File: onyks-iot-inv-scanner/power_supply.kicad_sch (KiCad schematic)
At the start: 47 parts, among them IC1 TPS22953DSQR, IC2 TPS22953DSQR, IC3 SN74LVC1G06DBVT, IC5 TPS63021DSJR, Q1 DMN3150L, Q2 DMN3150L, U1 DW01A, U3 TP4056-42-ESOP8, U4 TPS62A02ADRL, U5 TPS62A02ADRL

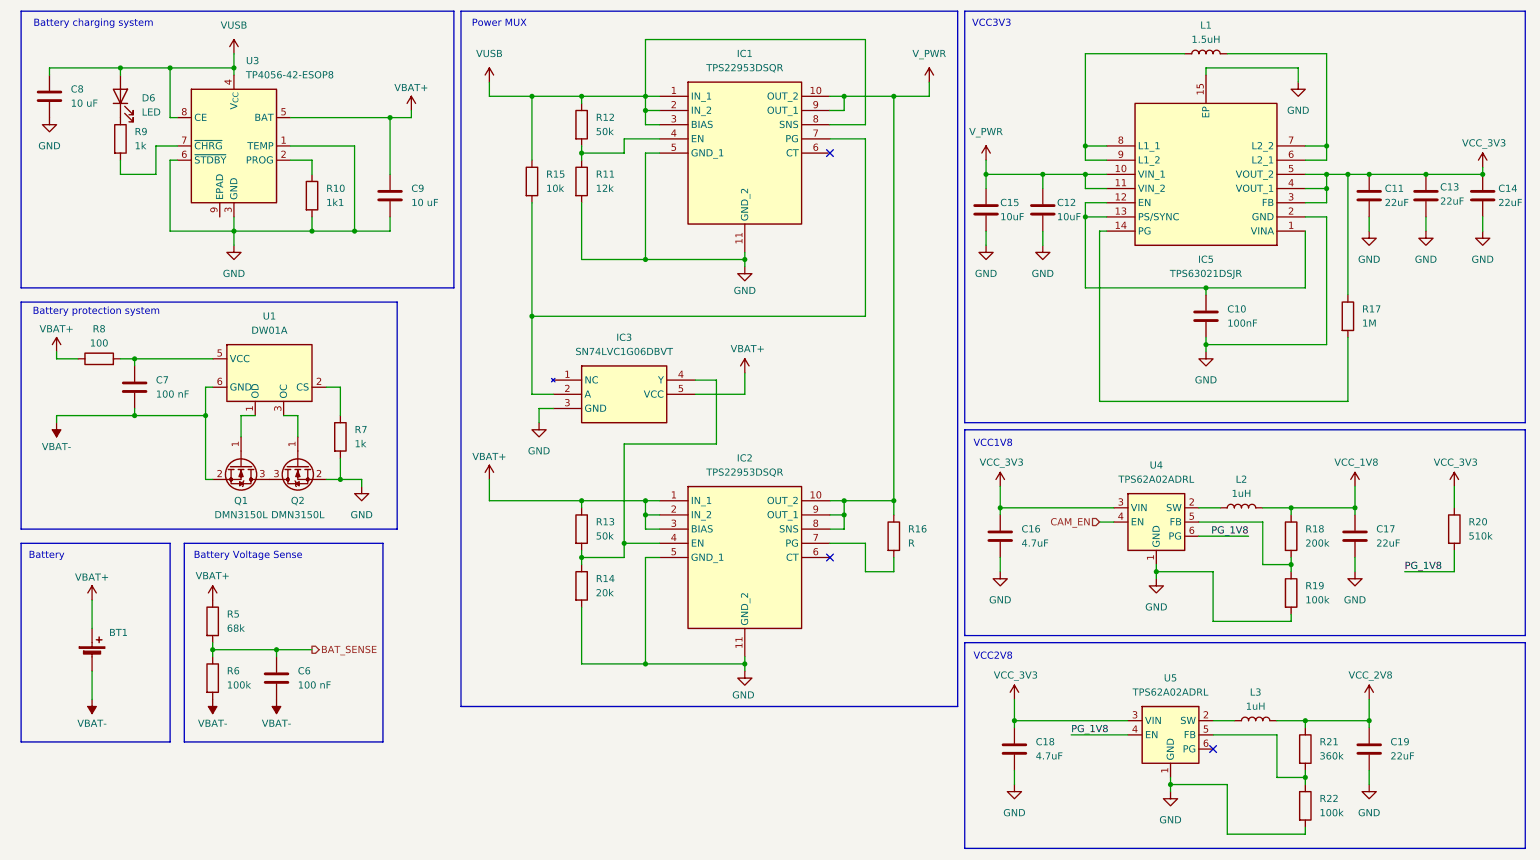
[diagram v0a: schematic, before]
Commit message: unpin usb data lines from battery management IC, becouse of possibly jamming signal
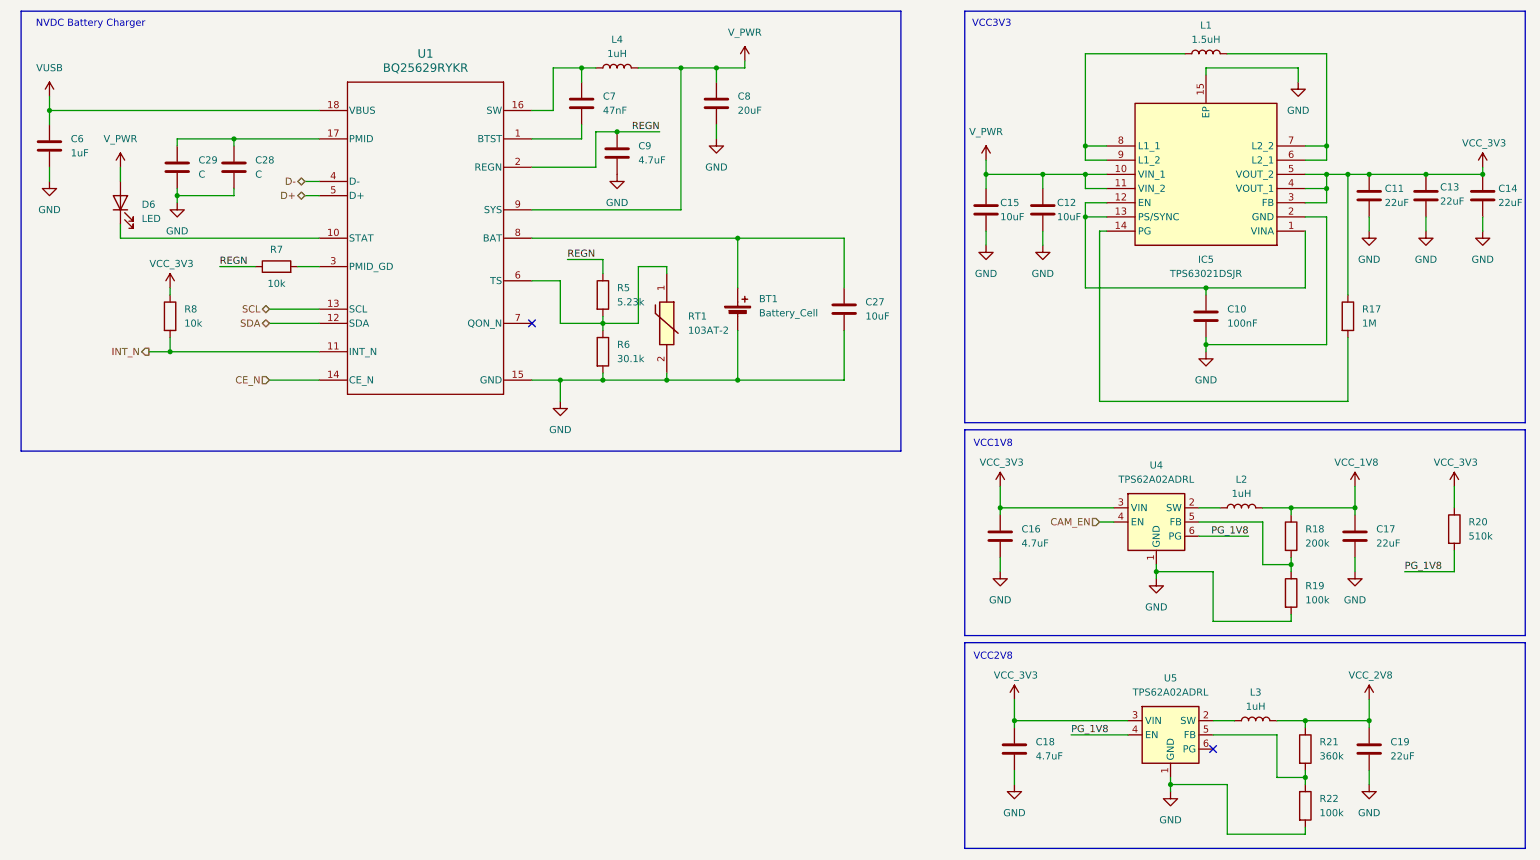
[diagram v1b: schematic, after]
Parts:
- removed IC1, IC2: TPS22953DSQR, Samacsys:SON40P200X200X80-11N, symbol Samacsys:TPS22953DSQR
- removed IC3: SN74LVC1G06DBVT, Samacsys:SOT95P280X145-5N, symbol Samacsys:SN74LVC1G06DBVT
- removed Q1, Q2: DMN3150L, Package_TO_SOT_SMD:SOT-23, symbol Transistor_FET:DMN3150L
- removed R10: 1k1, symbol Device:R
- removed R11: 12k, symbol Device:R
- removed R12, R13: 50k, symbol Device:R
- removed R14: 20k, symbol Device:R
- removed R15: 10k, symbol Device:R
- removed R16: R, symbol Device:R
- removed R9: 1k, symbol Device:R
- removed U1: DW01A, Package_TO_SOT_SMD:SOT-23-6, symbol Battery_Management:DW01A
- removed U3: TP4056-42-ESOP8, Package_SO:SOIC-8-1EP_3.9x4.9mm_P1.27mm_EP2.41x3.3mm_ThermalVias, symbol Battery_Management:TP4056-42-ESOP8
- added C27: 10uF, symbol Device:C
- added C28, C29: C, symbol Device:C
- added L4: 1uH, symbol Device:L
- added RT1: 103AT-2, Samacsys:103AT2, symbol Samacsys:103AT-2
- added U1: BQ25629RYKR, Snapeda:RYK0018A-MFG, symbol Snapeda:BQ25629RYKR
- C6: value 100 nF -> 1uF
- C7: value 100 nF -> 47nF
- C8: value 10 uF -> 20uF
- C9: value 10 uF -> 4.7uF
- R5: value 68k -> 5.23k
- R6: value 100k -> 30.1k
- R7: value 1k -> 10k
- R8: value 100 -> 10k
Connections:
- net GND: now also BT1.2 (-), C6.2, R6.2, C27.2, C28.2, C29.2, RT1.2, U1.15 (GND); no longer R7.2
- net VCC_3V3: now also R8.1
- net VUSB: now also C6.1, U1.18 (VBUS); no longer C8.1, D6.2 (A)
- net V_PWR: now also C8.1, D6.2 (A), L4.2, U1.9 (SYS)
- net REGN: now reaches R7.1
- net REGN: now also C9.1, R5.1, U1.2 (REGN)
- net at C7.1: now also L4.1, U1.16 (SW); no longer R8.2
- net at D6.1 (K): now also U1.10 (STAT)
- net BAT_SENSE: no longer names the net of R5.2, R6.1
- net BAT_SENSE: now also RT1.1, U1.6 (TS); no longer C6.1
- removed net VBAT+: BT1.1 (+), C9.1, R5.1, R8.1
- removed net VBAT-: BT1.2 (-), C6.2, C7.2, R6.2
- new net: BT1.1 (+), C27.1, U1.8 (BAT)
- new net: C28.1, C29.1, U1.17 (PMID)
- new net: R7.2, U1.3 (PMID_GD)
- new net: C7.2, U1.1 (BTST)
- new net CE_N: U1.14 (CE_N)
- new net D+: U1.5 (D+)
- new net D-: U1.4 (D-)
- new net INT_N: R8.2, U1.11 (INT_N)
- new net SCL: U1.13 (SCL)
- new net SDA: U1.12 (SDA)
- no-connect marks 3 -> 2
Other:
- note added: "NVDC Battery Charger"
- note removed: "Battery"
- note removed: "Battery Voltage Sense"
- note removed: "Battery charging system"
- note removed: "Battery protection system"
- note removed: "Power MUX"
